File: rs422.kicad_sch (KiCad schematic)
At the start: 4 parts, among them J10 Conn_02x04_Counter_Clockwise, U5 THVD1451D

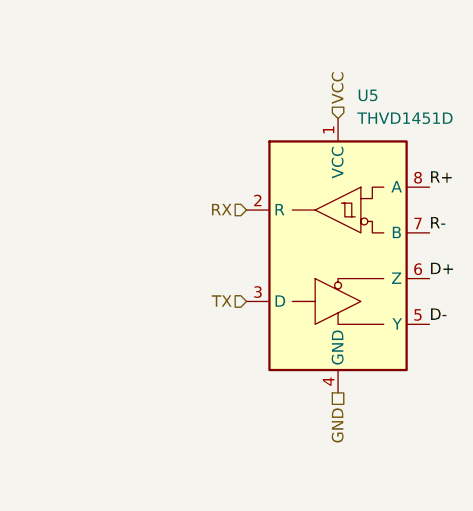
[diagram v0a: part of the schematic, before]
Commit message: pcb, sch: add transciever decoupling cap, docs, wireviz: add rs422 wiring harness
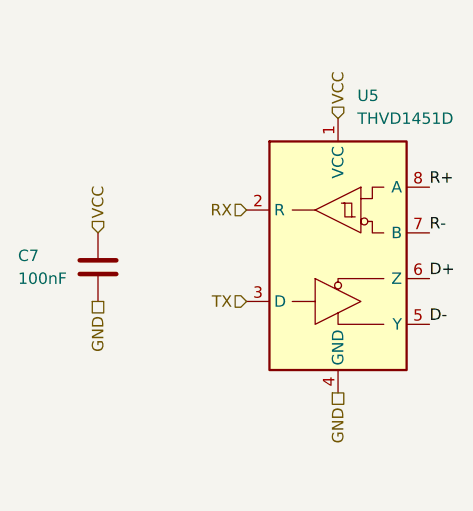
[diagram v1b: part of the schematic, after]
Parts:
- added C7: 100nF, Capacitor_SMD:C_0402_1005Metric, symbol Device:C
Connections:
- net GND: now also C7.1
- net VCC: now also C7.2
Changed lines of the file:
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@@
+	(hierarchical_label "GND"
+		(shape passive)
+		(at 97.79 93.98 270)
+		(effects
+			(font
+				(size 1.27 1.27)
+			)
+			(justify right)
+		)
+	)
 	(hierarchical_label "GND"
 		(shape passive)
@@
 		(shape input)
 		(at 124.46 73.66 90)
+		(effects
+			(font
+				(size 1.27 1.27)
+			)
+			(justify left)
+		)
+	)
+	(hierarchical_label "VCC"
+		(shape input)
+		(at 97.79 86.36 90)
 		(effects
 			(font
@@
 					(unit 1)
 				)
+			)
+		)
+	)
+	(symbol
+		(lib_id "Device:C")
+		(at 97.79 90.17 180)
+		(unit 1)
+		(exclude_from_sim no)
+		(in_bom yes)
+		(on_board yes)
+		(dnp no)
+		(property "Reference" "C7"
+			(at 88.9 88.9 0)
+			(effects
+				(font
+					(size 1.27 1.27)
+				)
+				(justify right)
+			)
+		)
+		(property "Value" "100nF"
+			(at 88.9 91.44 0)
+			(effects
+				(font
+					(size 1.27 1.27)
+				)
+				(justify right)
+			)
+		)
+		(property "Footprint" "Capacitor_SMD:C_0402_1005Metric"
+			(at 96.8248 86.36 0)
+			(effects
+				(font
+					(size 1.27 1.27)
+				)
+				(hide yes)
+			)
+		)
+		(property "Datasheet" "~"
+			(at 97.79 90.17 0)
+			(effects
+				(font
+					(size 1.27 1.27)
+				)
+				(hide yes)
+			)
+		)
+		(property "Description" "Unpolarized capacitor"
+			(at 97.79 90.17 0)
+			(effects
+				(font
+					(size 1.27 1.27)
+				)
+				(hide yes)
+			)
+		)
+		(pin "2"
+		)
+		(pin "1"
+		)
+		(instances
+			(project "P2 Kevinbot Board"
+				(path "/362ca48c-0b77-4943-b8b3-fc15ab97f30d/42a4c83c-2879-4a77-b31d-2d3ab7f5273b"
+					(reference "C7")
+					(unit 1)
+				)

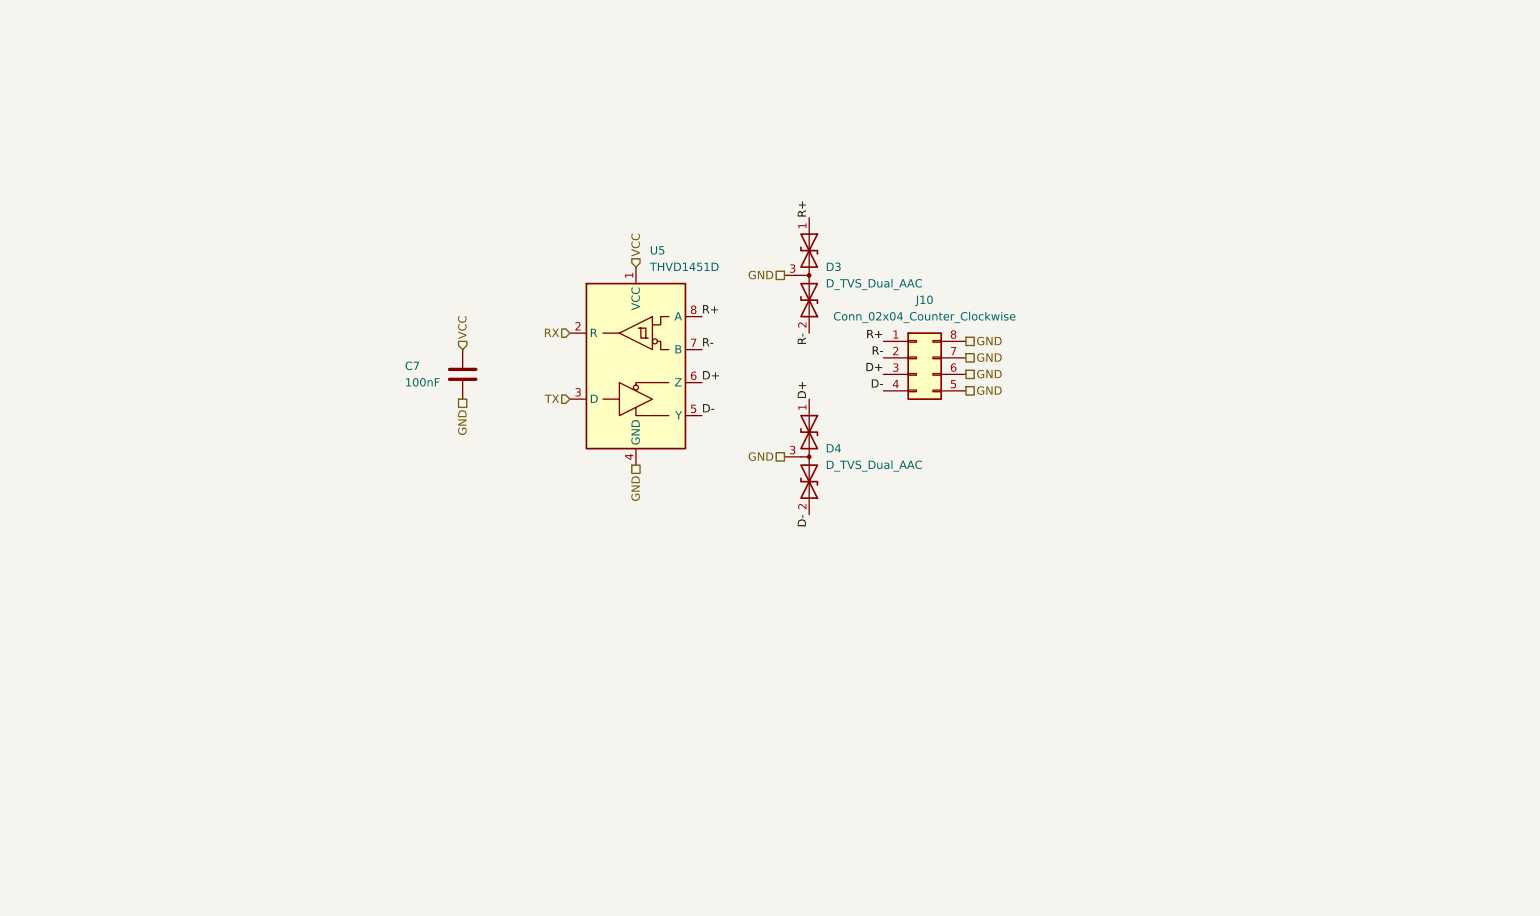
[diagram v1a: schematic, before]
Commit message: rs422, pcb: uart/rs422 mux
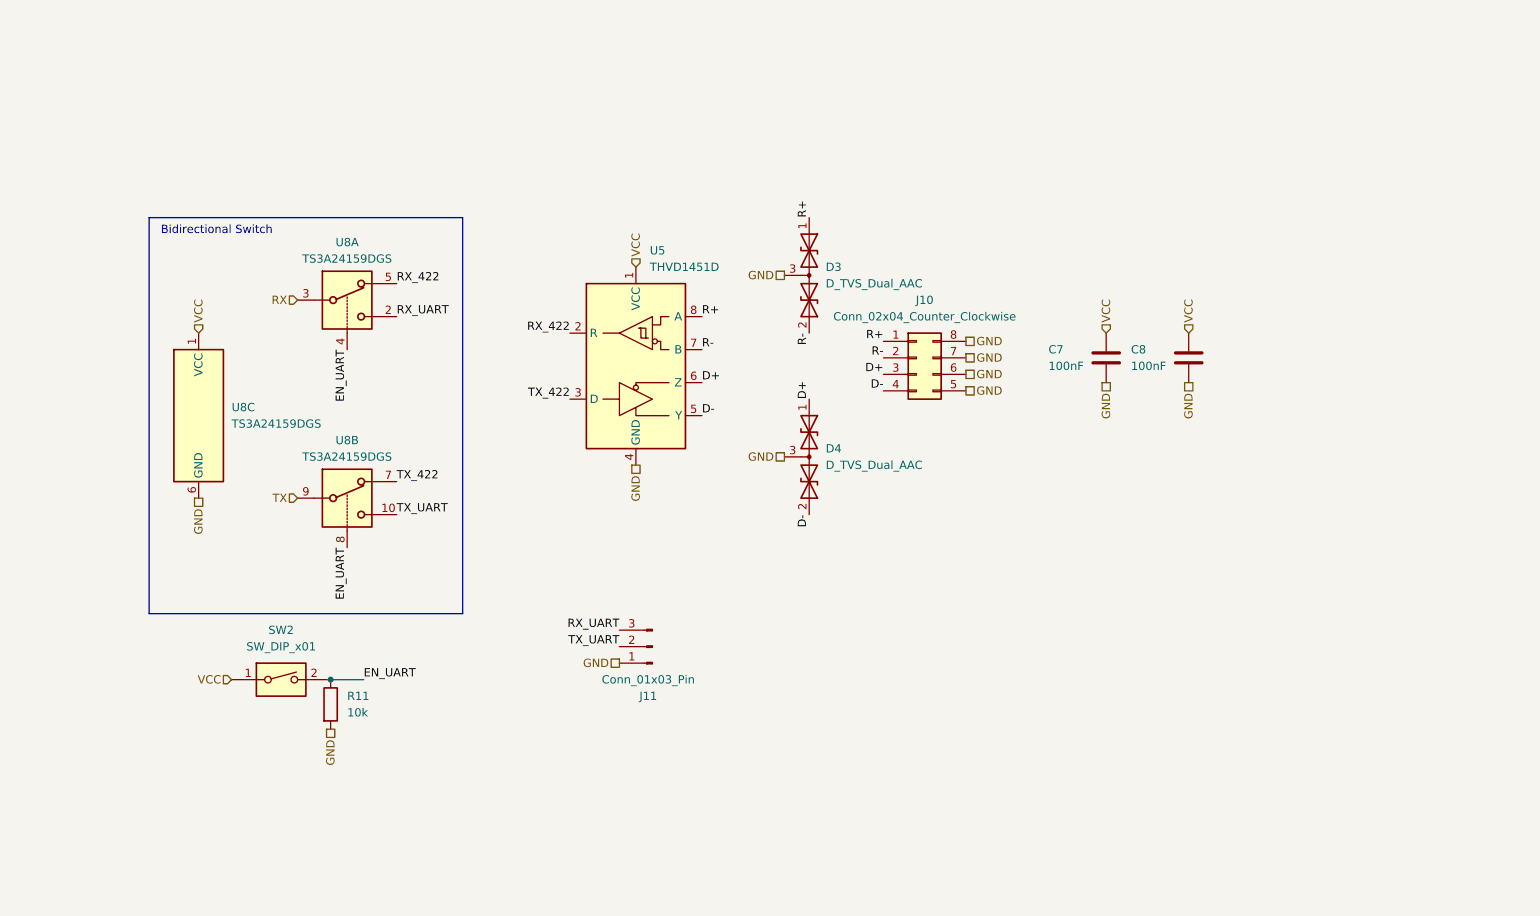
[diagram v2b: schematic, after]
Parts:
- added C8: 100nF, Capacitor_SMD:C_0402_1005Metric, symbol Device:C
- added J11: Conn_01x03_Pin, Connector_JST:JST_PH_B3B-PH-K_1x03_P2.00mm_Vertical, symbol Connector:Conn_01x03_Pin
- added R11: 10k, Resistor_SMD:R_0402_1005Metric, symbol Device:R
- added SW2: SW_DIP_x01, Button_Switch_SMD:SW_DIP_SPSTx01_Slide_Copal_CHS-01A_W5.08mm_P1.27mm_JPin, symbol Switch:SW_DIP_x01
- added U8: TS3A24159DGS, Package_SO:TSSOP-10_3x3mm_P0.5mm, symbol Analog_Switch:TS3A24159DGS
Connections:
- net GND: now also C8.1, J11.1 (Pin_1), R11.2, U8.6 (GND)
- net RX: now also U8.3; no longer U5.2 (R)
- net TX: now also U8.9; no longer U5.3 (D)
- net VCC: now also C8.2, SW2.1, U8.1 (VCC)
- new net EN_UART: R11.1, SW2.2, U8.4, U8.8
- new net RX_422: U5.2 (R), U8.5
- new net RX_UART: J11.3 (Pin_3), U8.2
- new net TX_422: U5.3 (D), U8.7
- new net TX_UART: J11.2 (Pin_2), U8.10
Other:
- note added: "Bidirectional Switch"
- moved on the sheet: C7

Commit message: sch, pcb: update pn fields
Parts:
- C7, C8: value 100nF -> 100nF 16v; Part Number (none) -> GRM155R71C104KA88D
- D3, D4: Part Number (none) -> D5V0L2B3SO-7
- J10: Part Number (none) -> 1053101108
- J11: Part Number (none) -> B3B-PH-K-S
- R11: Part Number (none) -> RC0402FR-0710KL
- SW2: Part Number (none) -> CHS-01A
- U8: Part Number (none) -> TS3A24159DGSR
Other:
- moved on the sheet: C7, C8
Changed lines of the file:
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@@
 	(hierarchical_label "GND"
 		(shape passive)
-		(at 196.85 91.44 270)
+		(at 214.63 87.63 270)
 		(effects
 			(font
@@
 	(hierarchical_label "GND"
 		(shape passive)
-		(at 209.55 91.44 270)
+		(at 214.63 109.22 270)
 		(effects
 			(font
@@
 	(hierarchical_label "VCC"
 		(shape input)
-		(at 209.55 83.82 90)
+		(at 214.63 101.6 90)
 		(effects
 			(font
@@
 	(hierarchical_label "VCC"
 		(shape input)
-		(at 196.85 83.82 90)
+		(at 214.63 80.01 90)
 		(effects
 			(font
@@
 			)
 		)
+		(property "Part Number" "TS3A24159DGSR"
+			(at 80.01 109.22 0)
+			(effects
+				(font
+					(size 1.27 1.27)
+				)
+				(hide yes)
+			)
+		)
 		(pin "6"
 		)
@@
 			)
 		)
+		(property "Part Number" "D5V0L2B3SO-7"
+			(at 151.13 102.87 90)
+			(effects
+				(font
+					(size 1.27 1.27)
+				)
+				(hide yes)
+			)
+		)
 		(pin "3"
 		)
@@
 			)
 		)
+		(property "Part Number" "TS3A24159DGSR"
+			(at 57.15 96.52 0)
+			(effects
+				(font
+					(size 1.27 1.27)
+				)
+				(hide yes)
+			)
+		)
 		(pin "6"
 		)
@@
 			)
 		)
+		(property "Part Number" "RC0402FR-0710KL"
+			(at 77.47 140.97 0)
+			(effects
+				(font
+					(size 1.27 1.27)
+				)
+				(hide yes)
+			)
+		)
 		(pin "1"
 		)
@@
 			)
 		)
+		(property "Part Number" "1053101108"
+			(at 167.64 87.63 0)
+			(effects
+				(font
+					(size 1.27 1.27)
+				)
+				(hide yes)
+			)
+		)
 		(pin "1"
 		)
@@
 	(symbol
 		(lib_id "Device:C")
-		(at 209.55 87.63 180)
+		(at 214.63 105.41 180)
 		(unit 1)
 		(exclude_from_sim no)
@@
 		(dnp no)
 		(property "Reference" "C8"
-			(at 200.66 86.36 0)
+			(at 205.74 104.14 0)
 			(effects
 				(font
@@
 			)
 		)
-		(property "Value" "100nF"
-			(at 200.66 88.9 0)
+		(property "Value" "100nF 16v"
+			(at 198.12 106.68 0)
 			(effects
 				(font
@@
 		)
 		(property "Footprint" "Capacitor_SMD:C_0402_1005Metric"
-			(at 208.5848 83.82 0)
+			(at 213.6648 101.6 0)
 			(effects
 				(font
@@
 		)
 		(property "Datasheet" "~"
-			(at 209.55 87.63 0)
+			(at 214.63 105.41 0)
 			(effects
 				(font
@@
 		)
 		(property "Description" "Unpolarized capacitor"
-			(at 209.55 87.63 0)
+			(at 214.63 105.41 0)
+			(effects
+				(font
+					(size 1.27 1.27)
+				)
+				(hide yes)
+			)
+		)
+		(property "Part Number" "GRM155R71C104KA88D"
+			(at 214.63 105.41 0)
 			(effects
 				(font
@@
 			)
 		)
+		(property "Part Number" "B3B-PH-K-S"
+			(at 127 132.08 0)
+			(effects
+				(font
+					(size 1.27 1.27)
+				)
+				(hide yes)
+			)
+		)
 		(pin "1"
 		)
@@
 			)
 		)
+		(property "Part Number" "TS3A24159DGSR"
+			(at 80.01 78.74 0)
+			(effects
+				(font
+					(size 1.27 1.27)
+				)
+				(hide yes)
+			)
+		)
 		(pin "6"
 		)
@@
 			)
 		)
+		(property "Part Number" "D5V0L2B3SO-7"
+			(at 151.13 74.93 90)
+			(effects
+				(font
+					(size 1.27 1.27)
+				)
+				(hide yes)
+			)
+		)
 		(pin "3"
 		)
@@
 	(symbol
 		(lib_id "Device:C")
-		(at 196.85 87.63 180)
+		(at 214.63 83.82 180)
 		(unit 1)
 		(exclude_from_sim no)
@@
 		(dnp no)
 		(property "Reference" "C7"
-			(at 187.96 86.36 0)
+			(at 205.74 82.55 0)
 			(effects
 				(font
@@
 			)
 		)
-		(property "Value" "100nF"
-			(at 187.96 88.9 0)
+		(property "Value" "100nF 16v"
+			(at 197.866 85.09 0)
 			(effects
 				(font
@@
 		)
 		(property "Footprint" "Capacitor_SMD:C_0402_1005Metric"
-			(at 195.8848 83.82 0)
+			(at 213.6648 80.01 0)
 			(effects
 				(font
@@
 		)
 		(property "Datasheet" "~"
-			(at 196.85 87.63 0)
+			(at 214.63 83.82 0)
 			(effects
 				(font
@@
 		)
 		(property "Description" "Unpolarized capacitor"
-			(at 196.85 87.63 0)
+			(at 214.63 83.82 0)
+			(effects
+				(font
+					(size 1.27 1.27)
+				)
+				(hide yes)
+			)
+		)
+		(property "Part Number" "GRM155R71C104KA88D"
+			(at 214.63 83.82 0)
 			(effects
 				(font
@@
 			(at 69.85 137.16 0)
 			(effects
+				(font
+					(size 1.27 1.27)
+				)
+				(hide yes)
+			)
+		)
+		(property "Part Number" "CHS-01A"
+			(at 69.85 137.16 0)
+			(effects

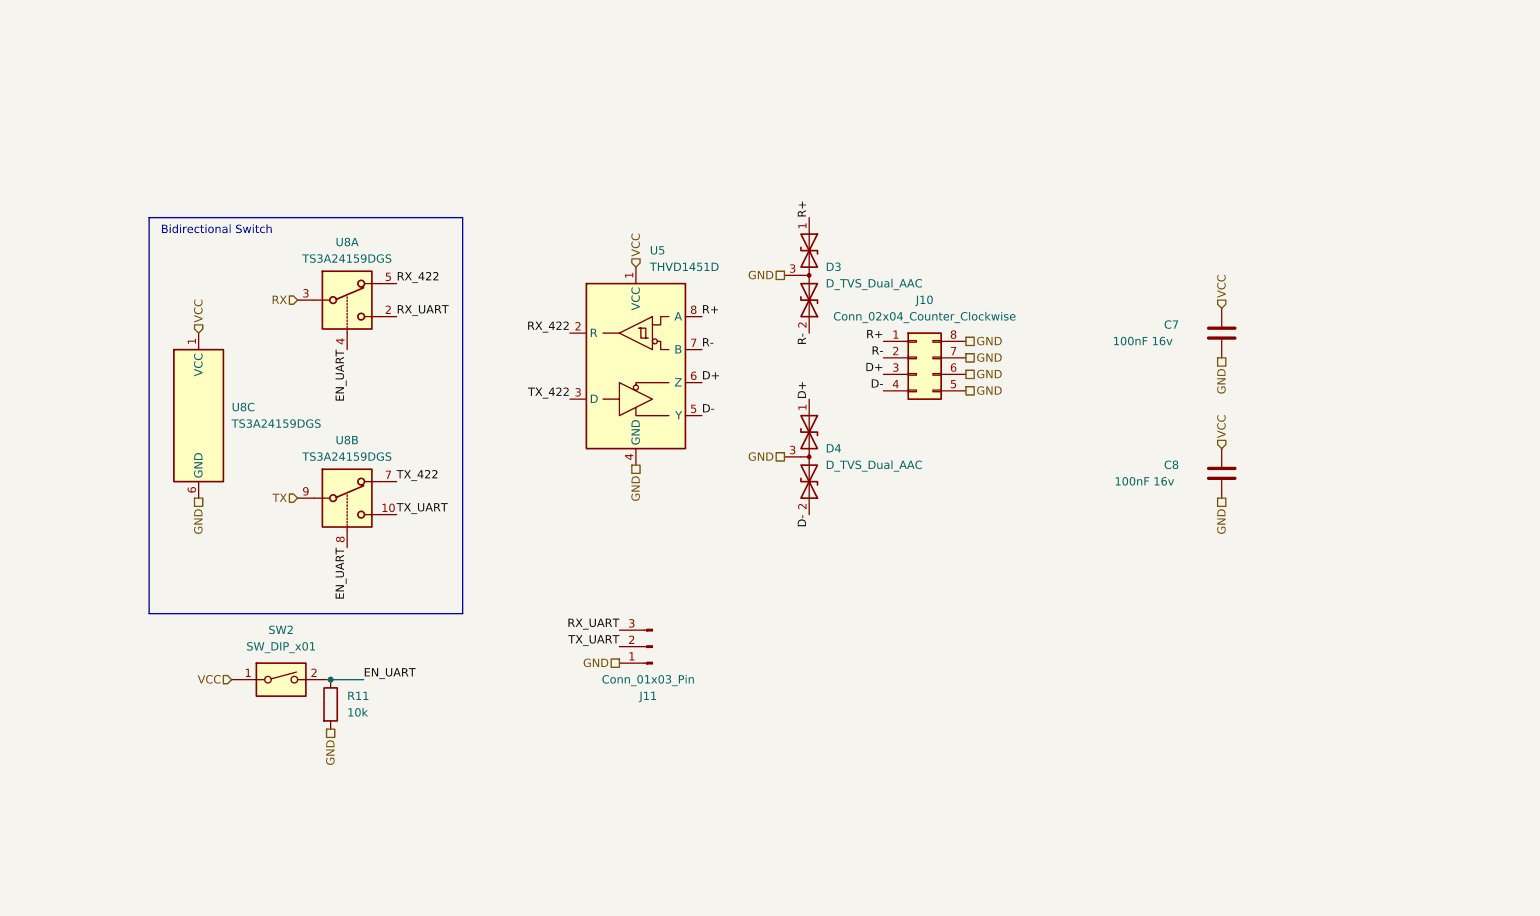
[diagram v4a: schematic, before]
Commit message: i2c, servo, pcb: pca9685 servo, pcb, rs422: leds
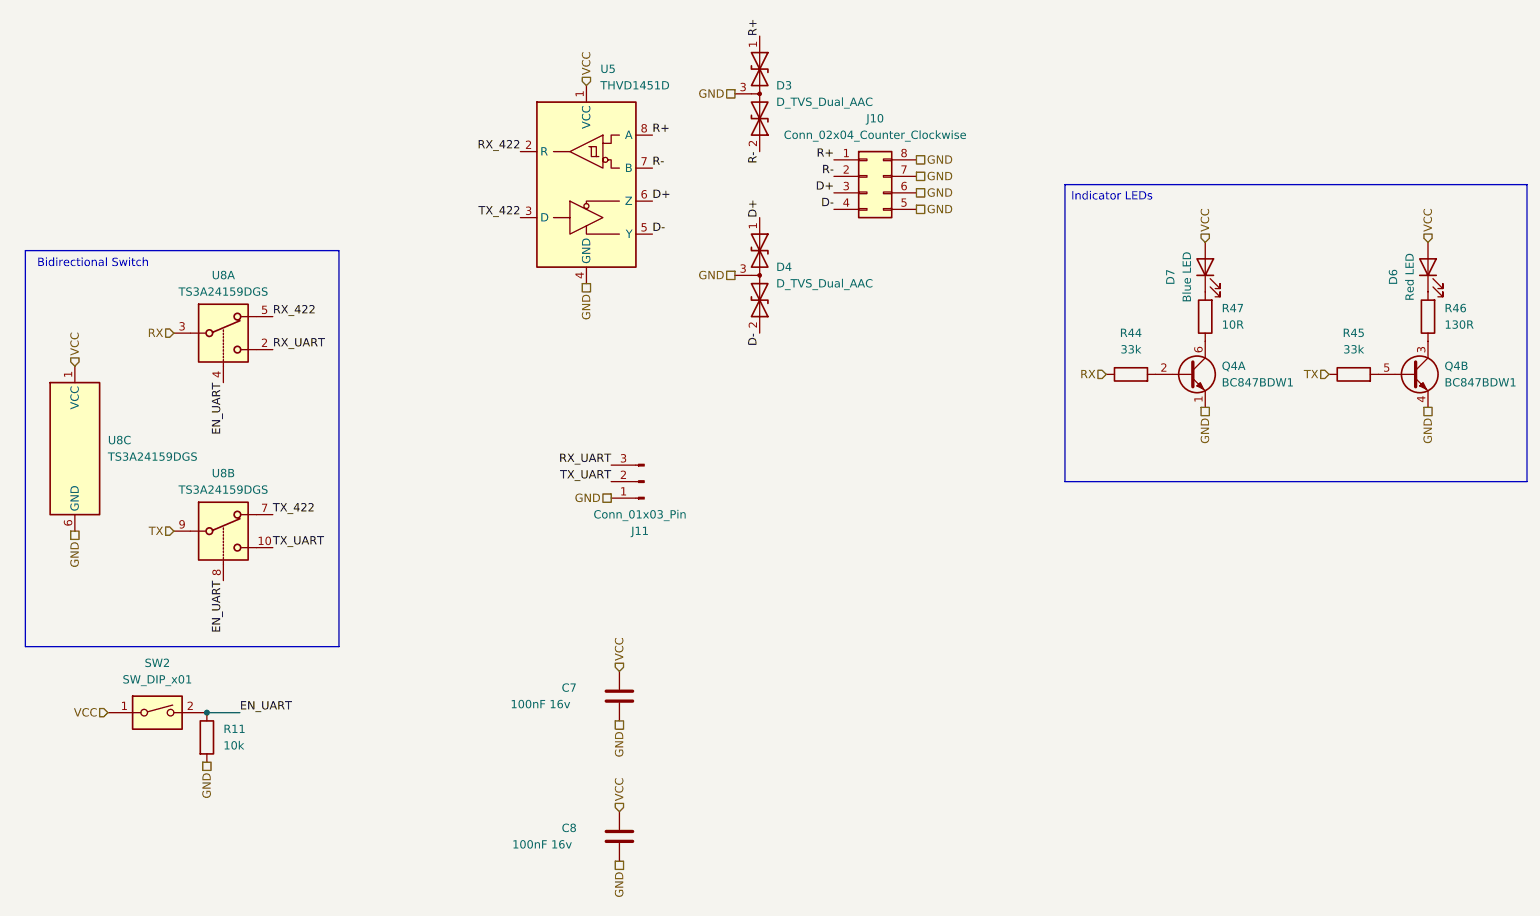
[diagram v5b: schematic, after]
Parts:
- added D6: Red LED, LED_SMD:LED_0603_1608Metric, symbol Device:LED
- added D7: Blue LED, LED_SMD:LED_0603_1608Metric, symbol Device:LED
- added Q4: BC847BDW1, Package_TO_SOT_SMD:SOT-363_SC-70-6, symbol Transistor_BJT:BC847BDW1
- added R44, R45: 33k, Resistor_SMD:R_0402_1005Metric, symbol Device:R
- added R46: 130R, Resistor_SMD:R_0402_1005Metric, symbol Device:R
- added R47: 10R, Resistor_SMD:R_0402_1005Metric, symbol Device:R
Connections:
- net GND: now also Q4.1 (E1), Q4.4 (E2)
- net RX: now also R44.1
- net TX: now also R45.1
- net VCC: now also D6.2 (A), D7.2 (A)
- new net: Q4.5 (B2), R45.2
- new net: Q4.2 (B1), R44.2
- new net: Q4.6 (C1), R47.1
- new net: D6.1 (K), R46.2
- new net: Q4.3 (C2), R46.1
- new net: D7.1 (K), R47.2
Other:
- moved on the sheet: C7, C8, D3, D4, J10, J11, R11, SW2, U5, U8A, U8B, U8C
